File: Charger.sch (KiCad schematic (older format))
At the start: 84 parts, among them Q1 VBA2625, Q10 AON7400A, Q11 AON7400A, Q14 2n7002K, Q15 VBA2625, Q8 AON7400A, Q9 AON7400A, U1 BQ25703ARSNR

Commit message: Much layout. Wow
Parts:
- removed Q10, Q11, Q9: AON7400A, lc_lib:QFN-8_3X3X065P, symbol SmartBattery:AO4468
- added Q10, Q11, Q9: AON7400A, lc_lib:SON-8_3.3X3.3MM, symbol SmartBattery:AON7400A
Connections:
- net VSYS: now also Q11.5 (D), Q11.6 (D), Q11.7 (D), Q11.8 (D)
- net at C15.2, C17.2, C37.1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: now also Q9.5 (D), Q9.6 (D), Q9.7 (D), Q9.8 (D)
- net at C46.1, L1.1, U1.23 (SW2): now also Q10.5 (D), Q10.6 (D), Q10.7 (D), Q10.8 (D), Q11.1 (S), Q11.2 (S), Q11.3 (S)
- net at C43.1, L1.2, Q8.0 (D)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: now also Q9.1 (S), Q9.2 (S), Q9.3 (S)
- net at R38.1: now also Q9.4 (G)
- net at R54.2: now also Q11.4 (G)
- new net: Q10.1 (S), Q10.2 (S), Q10.3 (S)
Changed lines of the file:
@@
-$EndComp
-$Comp
-L SmartBattery:AO4468 Q9
-U 1 1 60390F2A
-P 4050 1950
-F 0 "Q9" V 4393 1950 50  0000 C CNN
-F 1 "AON7400A " V 4302 1950 50  0000 C CNN
-F 2 "lc_lib:QFN-8_3X3X065P" H 4250 2050 50  0001 C CNN
-F 3 "~" H 4050 1950 50  0001 C CNN
-F 4 " C85734" V 4050 1950 50  0001 C CNN "LCSC"
-	1    4050 1950
-	0    -1   -1   0
-$EndComp
-$Comp
-L SmartBattery:AO4468 Q11
-U 1 1 603A292B
-P 6400 2450
-F 0 "Q11" H 6606 2496 50  0000 L CNN
-F 1 "AON7400A " H 6606 2405 50  0000 L CNN
-F 2 "lc_lib:QFN-8_3X3X065P" H 6600 2550 50  0001 C CNN
-F 3 "~" H 6400 2450 50  0001 C CNN
-F 4 "C85734" H 6400 2450 50  0001 C CNN "LCSC"
-	1    6400 2450
-	1    0    0    1
 $EndComp
 $Comp
@@
 	5200 2650 5200 2900
 $Comp
-L SmartBattery:AO4468 Q10
-U 1 1 603A12F1
-P 5600 2050
-F 0 "Q10" H 5806 2096 50  0000 L CNN
-F 1 "AON7400A " H 5806 2005 50  0000 L CNN
-F 2 "lc_lib:QFN-8_3X3X065P" H 5800 2150 50  0001 C CNN
-F 3 "~" H 5600 2050 50  0001 C CNN
-F 4 "C85734" H 5600 2050 50  0001 C CNN "LCSC"
-	1    5600 2050
-	1    0    0    -1
-$EndComp
-$Comp
 L Device:C_Small C51
 U 1 1 6081E24F
@@
 	0    1    1    0
 $EndComp
-Wire Wire Line
-	5200 1850 5700 1850
-Connection ~ 5700 1850
 $Comp
 L power:GND #PWR0128
@@
 Wire Wire Line
 	5750 2250 5700 2250
-Connection ~ 5700 2250
 Wire Wire Line
 	5500 2250 5450 2250
@@
 Wire Wire Line
 	6500 1850 6500 2250
-Wire Wire Line
-	5700 1850 6500 1850
 Wire Wire Line
 	5450 3200 5950 3200
@@
 Wire Wire Line
 	7300 3400 7250 3400
+$Comp
+L SmartBattery:AON7400A Q?
+U 1 1 60093DF8
+P 4050 1950
+AR Path="/5FD15753/60093DF8" Ref="Q?"  Part="1"
+AR Path="/5FD99B08/60093DF8" Ref="Q9"  Part="1"
+F 0 "Q9" V 4400 2100 50  0000 L CNN
+F 1 "AON7400A" V 4300 1900 50  0000 L CNN
+F 2 "lc_lib:SON-8_3.3X3.3MM" H 4700 2400 50  0001 C CNN
+F 3 "~" H 4050 1950 50  0001 C CNN
+F 4 "AON7400A" H 4256 1905 50  0001 L CNN "SKU"
+F 5 "C85734" H 4256 1814 50  0001 L CNN "LCSC"
+	1    4050 1950
+	0    -1   -1   0
+$EndComp
+$Comp
+L SmartBattery:AON7400A Q?
+U 1 1 600966B5
+P 5550 2050
+AR Path="/5FD15753/600966B5" Ref="Q?"  Part="1"
+AR Path="/5FD99B08/600966B5" Ref="Q10"  Part="1"
+F 0 "Q10" V 5900 2200 50  0000 L CNN
+F 1 "AON7400A" V 5800 2000 50  0000 L CNN
+F 2 "lc_lib:SON-8_3.3X3.3MM" H 6200 2500 50  0001 C CNN
+F 3 "~" H 5550 2050 50  0001 C CNN
+F 4 "AON7400A" H 5756 2005 50  0001 L CNN "SKU"
+F 5 "C85734" H 5756 1914 50  0001 L CNN "LCSC"
+	1    5550 2050
+	1    0    0    -1
+$EndComp
+$Comp
+L SmartBattery:AON7400A Q?
+U 1 1 600C3E3E
+P 6400 2450
+AR Path="/5FD15753/600C3E3E" Ref="Q?"  Part="1"
+AR Path="/5FD99B08/600C3E3E" Ref="Q11"  Part="1"
+F 0 "Q11" V 6750 2600 50  0000 L CNN
+F 1 "AON7400A" V 6650 2400 50  0000 L CNN
+F 2 "lc_lib:SON-8_3.3X3.3MM" H 7050 2900 50  0001 C CNN
+F 3 "~" H 6400 2450 50  0001 C CNN
+F 4 "AON7400A" H 6606 2405 50  0001 L CNN "SKU"
+F 5 "C85734" H 6606 2314 50  0001 L CNN "LCSC"
+	1    6400 2450
+	1    0    0    1
+$EndComp
+Wire Wire Line
+	5200 1850 5650 1850
+Connection ~ 5650 1850
+Wire Wire Line
+	5650 1850 6500 1850
 $EndSCHEMATC

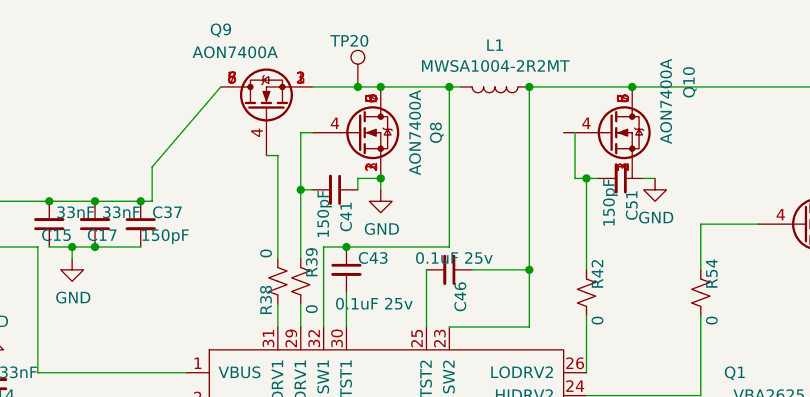
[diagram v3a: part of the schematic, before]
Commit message: Layout placed type-c + barrel jack
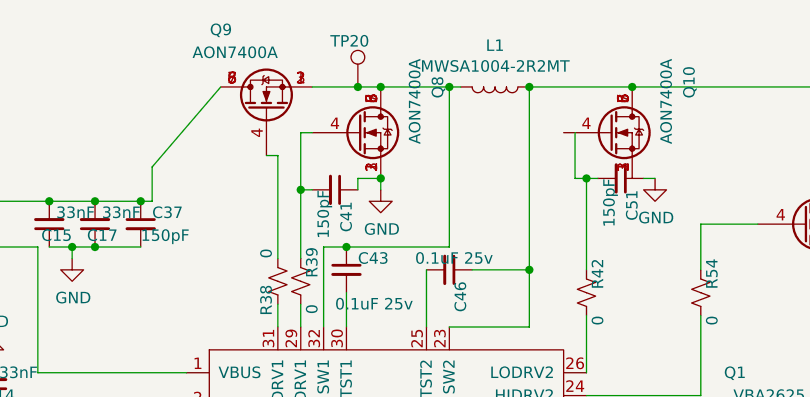
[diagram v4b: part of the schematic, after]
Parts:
- removed Q8: AON7400A, lc_lib:QFN-8_3X3X065P, symbol SmartBattery:AO4468
- added Q8: AON7400A, lc_lib:SON-8_3.3X3.3MM, symbol SmartBattery:AON7400A
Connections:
- net GND: now also Q8.1 (S), Q8.2 (S), Q8.3 (S)
- net at C43.1, L1.2, Q9.1 (S)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: now also Q8.5 (D), Q8.6 (D), Q8.7 (D), Q8.8 (D)
- net at C41.2, R39.2: now also Q8.4 (G)
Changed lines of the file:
@@
 	3500 2550 3300 2550
 Connection ~ 3300 2550
-$Comp
-L SmartBattery:AO4468 Q8
-U 1 1 6038DB58
-P 4450 2050
-F 0 "Q8" V 4793 2050 50  0000 C CNN
-F 1 "AON7400A " V 4702 2050 50  0000 C CNN
-F 2 "lc_lib:QFN-8_3X3X065P" H 4650 2150 50  0001 C CNN
-F 3 "~" H 4450 2050 50  0001 C CNN
-F 4 "C85734" V 4450 2050 50  0001 C CNN "LCSC"
-	1    4450 2050
-	1    0    0    -1
-$EndComp
 Wire Wire Line
 	3550 2350 3550 2200
@@
 Wire Wire Line
 	4450 2250 4450 2300
-Connection ~ 4550 2250
 Wire Wire Line
 	4250 2300 4200 2300
@@
 $EndComp
 Connection ~ 4450 1850
-Wire Wire Line
-	4450 1850 4550 1850
-Wire Wire Line
-	4550 1850 4850 1850
-Connection ~ 4550 1850
 Wire Wire Line
 	4300 2900 4300 2550
@@
 Wire Wire Line
 	5650 1850 6500 1850
+$Comp
+L SmartBattery:AON7400A Q?
+U 1 1 600EE040
+P 4450 2050
+AR Path="/5FD15753/600EE040" Ref="Q?"  Part="1"
+AR Path="/5FD99B08/600EE040" Ref="Q8"  Part="1"
+F 0 "Q8" V 4800 2200 50  0000 L CNN
+F 1 "AON7400A" V 4700 2000 50  0000 L CNN
+F 2 "lc_lib:SON-8_3.3X3.3MM" H 5100 2500 50  0001 C CNN
+F 3 "~" H 4450 2050 50  0001 C CNN
+F 4 "AON7400A" H 4656 2005 50  0001 L CNN "SKU"
+F 5 "C85734" H 4656 1914 50  0001 L CNN "LCSC"
+	1    4450 2050
+	1    0    0    -1
+$EndComp
+Wire Wire Line
+	4450 1850 4550 1850
+Connection ~ 4550 2250
+Connection ~ 4550 1850
+Wire Wire Line
+	4550 1850 4850 1850
 $EndSCHEMATC

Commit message: Much layout wow.
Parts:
- removed C16, C89: 220u, Capacitor_SMD:C_Elec_8x10.2, symbol Device:C_Small
- added C147, C16, C89: 220u, Capacitor_SMD:C_Elec_8x10.2, symbol Device:CP_Small
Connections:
- net ADAPTER_IN: now also C147.1
- net GND: now also Q10.1 (S), Q10.2 (S), Q10.3 (S), C147.2, C16.2, C89.2
- net VSYS: now also C16.1, C89.1
- net at Q10.4 (G): now also C51.2, R42.2
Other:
- moved on the sheet: C51
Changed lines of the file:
@@
 	0    -1   -1   0
-$EndComp
-$Comp
-L Device:C_Small C16
-U 1 1 5FDC314F
-P 7950 2800
-F 0 "C16" H 8042 2846 50  0000 L CNN
-F 1 "220u" H 8042 2755 50  0000 L CNN
-F 2 "Capacitor_SMD:C_Elec_8x10.2" H 7950 2800 50  0001 C CNN
-F 3 "~" H 7950 2800 50  0001 C CNN
-F 4 "C311611" H 7950 2800 50  0001 C CNN "LCSC"
-	1    7950 2800
-	1    0    0    -1
 $EndComp
 Text HLabel 8400 2500 2    50   BiDi ~ 0
@@
 L Device:C_Small C51
 U 1 1 6081E24F
-P 5600 2250
-F 0 "C51" H 5650 2300 50  0000 L CNN
-F 1 "150pF" H 5600 2200 50  0000 L CNN
-F 2 "lc_lib:0402_C" H 5600 2250 50  0001 C CNN
-F 3 "~" H 5600 2250 50  0001 C CNN
-F 4 "C1527" H 5600 2250 50  0001 C CNN "lcsc"
-	1    5600 2250
+P 5550 2350
+F 0 "C51" H 5600 2400 50  0000 L CNN
+F 1 "150pF" H 5550 2300 50  0000 L CNN
+F 2 "lc_lib:0402_C" H 5550 2350 50  0001 C CNN
+F 3 "~" H 5550 2350 50  0001 C CNN
+F 4 "C1527" H 5550 2350 50  0001 C CNN "lcsc"
+	1    5550 2350
 	0    1    1    0
 $EndComp
@@
 $EndComp
 Wire Wire Line
-	5750 2250 5700 2250
-Wire Wire Line
-	5500 2250 5450 2250
-Wire Wire Line
 	5400 2250 5400 2050
 Wire Wire Line
 	5450 3100 5450 2850
-Connection ~ 5450 2250
 Wire Wire Line
 	5450 2250 5400 2250
@@
 $EndComp
 Wire Wire Line
-	5450 2650 5450 2250
+	5450 2650 5450 2350
 $Comp
 L Device:R_Small_US R54
@@
 	1    0    0    -1
 $EndComp
-$Comp
-L Device:C_Small C89
-U 1 1 60904FCD
-P 8300 2800
-F 0 "C89" H 8392 2846 50  0000 L CNN
-F 1 "220u" H 8392 2755 50  0000 L CNN
-F 2 "Capacitor_SMD:C_Elec_8x10.2" H 8300 2800 50  0001 C CNN
-F 3 "~" H 8300 2800 50  0001 C CNN
-F 4 "C311611" H 8300 2800 50  0001 C CNN "LCSC"
-	1    8300 2800
-	1    0    0    -1
-$EndComp
 Wire Wire Line
 	6800 2900 6950 2900
@@
 Wire Wire Line
 	7700 2900 7800 2900
-Connection ~ 7950 2900
-Wire Wire Line
-	7950 2900 8300 2900
 Wire Wire Line
 	7250 2700 7400 2700
@@
 	7400 2700 7500 2700
 Connection ~ 7700 2700
-Wire Wire Line
-	7700 2700 7950 2700
-Connection ~ 7950 2700
-Wire Wire Line
-	7950 2700 8300 2700
 $Comp
 L power:GND #PWR0129
@@
 $EndComp
 Connection ~ 7800 2900
-Wire Wire Line
-	7800 2900 7950 2900
 Connection ~ 7500 2700
 Wire Wire Line
@@
 Wire Wire Line
 	8300 2500 8400 2500
-Connection ~ 8300 2700
 Wire Wire Line
 	6800 3400 6550 3400
@@
 Wire Wire Line
 	4550 1850 4850 1850
+Wire Wire Line
+	2400 3550 2600 3550
+Connection ~ 2400 3550
+Wire Wire Line
+	2600 3750 2400 3750
+Connection ~ 2400 3750
+$Comp
+L Device:CP_Small C?
+U 1 1 600ECC91
+P 2600 3650
+AR Path="/60413DD6/600ECC91" Ref="C?"  Part="1"
+AR Path="/5FD99B08/600ECC91" Ref="C147"  Part="1"
+F 0 "C147" H 2500 3700 50  0000 R CNN
+F 1 "220u" H 2450 3600 50  0000 R CNN
+F 2 "Capacitor_SMD:C_Elec_8x10.2" H 2600 3650 50  0001 C CNN
+F 3 "~" H 2600 3650 50  0001 C CNN
+F 4 "C311611" H 2600 3650 50  0001 C CNN "LCSC"
+	1    2600 3650
+	-1   0    0    -1
+$EndComp
+$Comp
+L Device:CP_Small C?
+U 1 1 600F8E33
+P 8000 2800
+AR Path="/60413DD6/600F8E33" Ref="C?"  Part="1"
+AR Path="/5FD99B08/600F8E33" Ref="C16"  Part="1"
+F 0 "C16" H 7900 2850 50  0000 R CNN
+F 1 "220u" H 7900 2750 50  0000 R CNN
+F 2 "Capacitor_SMD:C_Elec_8x10.2" H 8000 2800 50  0001 C CNN
+F 3 "~" H 8000 2800 50  0001 C CNN
+F 4 "C311611" H 8000 2800 50  0001 C CNN "LCSC"
+	1    8000 2800
+	-1   0    0    -1
+$EndComp
+$Comp
+L Device:CP_Small C?
+U 1 1 600FA944
+P 8300 2800
+AR Path="/60413DD6/600FA944" Ref="C?"  Part="1"
+AR Path="/5FD99B08/600FA944" Ref="C89"  Part="1"
+F 0 "C89" H 8200 2850 50  0000 R CNN
+F 1 "220u" H 8150 2750 50  0000 R CNN
+F 2 "Capacitor_SMD:C_Elec_8x10.2" H 8300 2800 50  0001 C CNN
+F 3 "~" H 8300 2800 50  0001 C CNN
+F 4 "C311611" H 8300 2800 50  0001 C CNN "LCSC"
+	1    8300 2800
+	-1   0    0    -1
+$EndComp
+Wire Wire Line
+	7700 2700 8000 2700
+Wire Wire Line
+	7800 2900 8000 2900
+Connection ~ 8000 2700
+Wire Wire Line
+	8000 2700 8300 2700
+Connection ~ 8000 2900
+Wire Wire Line
+	8000 2900 8300 2900
+Connection ~ 8300 2700
+Wire Wire Line
+	5400 2050 5350 2050
+Connection ~ 5450 2350
+Wire Wire Line
+	5450 2350 5450 2250
+Wire Wire Line
+	5650 2250 5750 2250
+Connection ~ 5650 2250
+Wire Wire Line
+	5650 2250 5650 2350
 $EndSCHEMATC

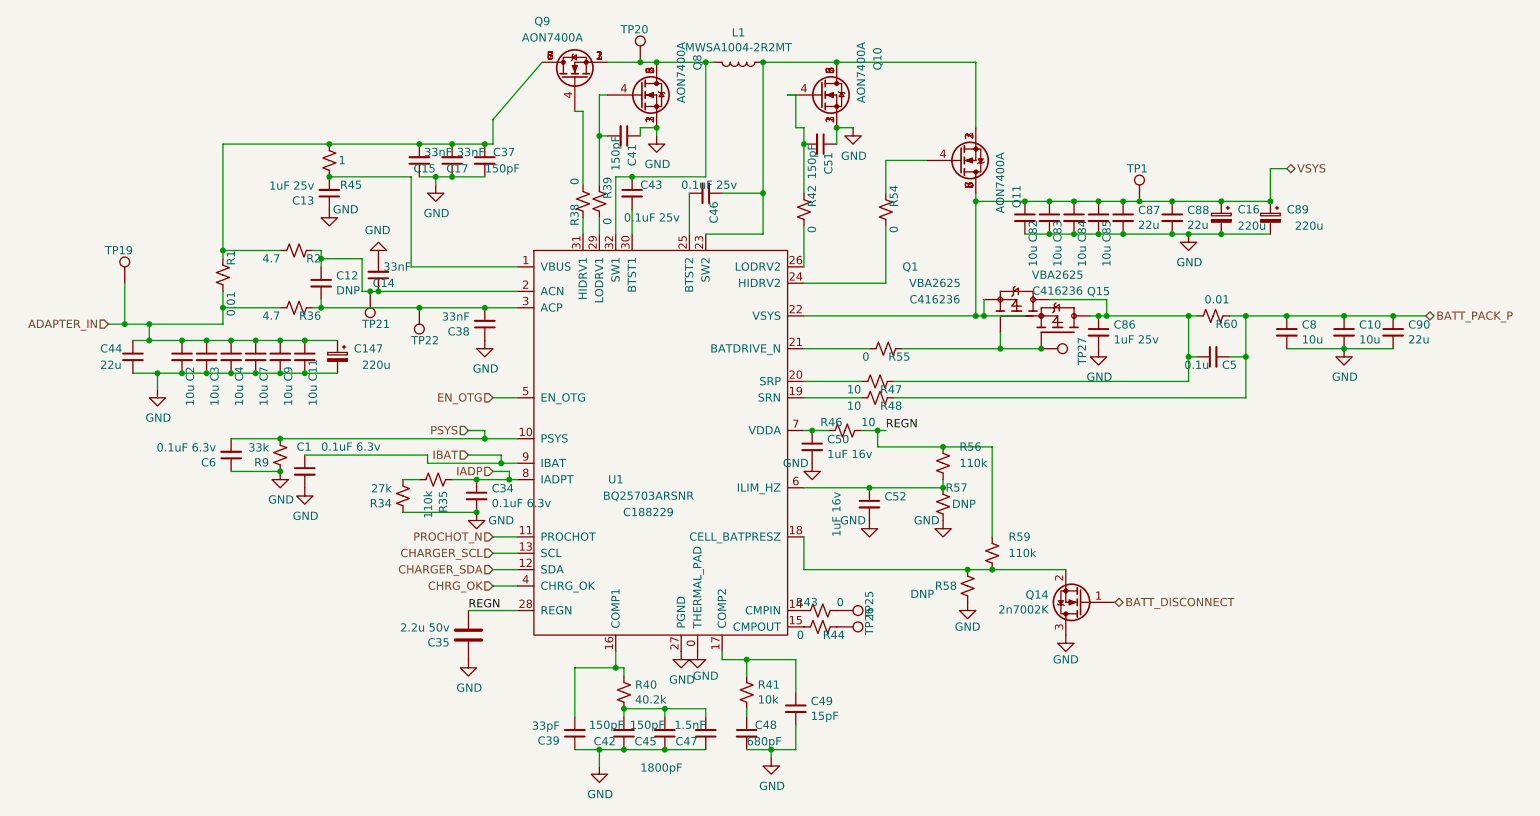
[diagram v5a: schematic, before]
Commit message: Almost connected MCU + ESP32 added leds addedd uart usb cleaned up type-c I/O -- STILL NEED TO level shift I2C
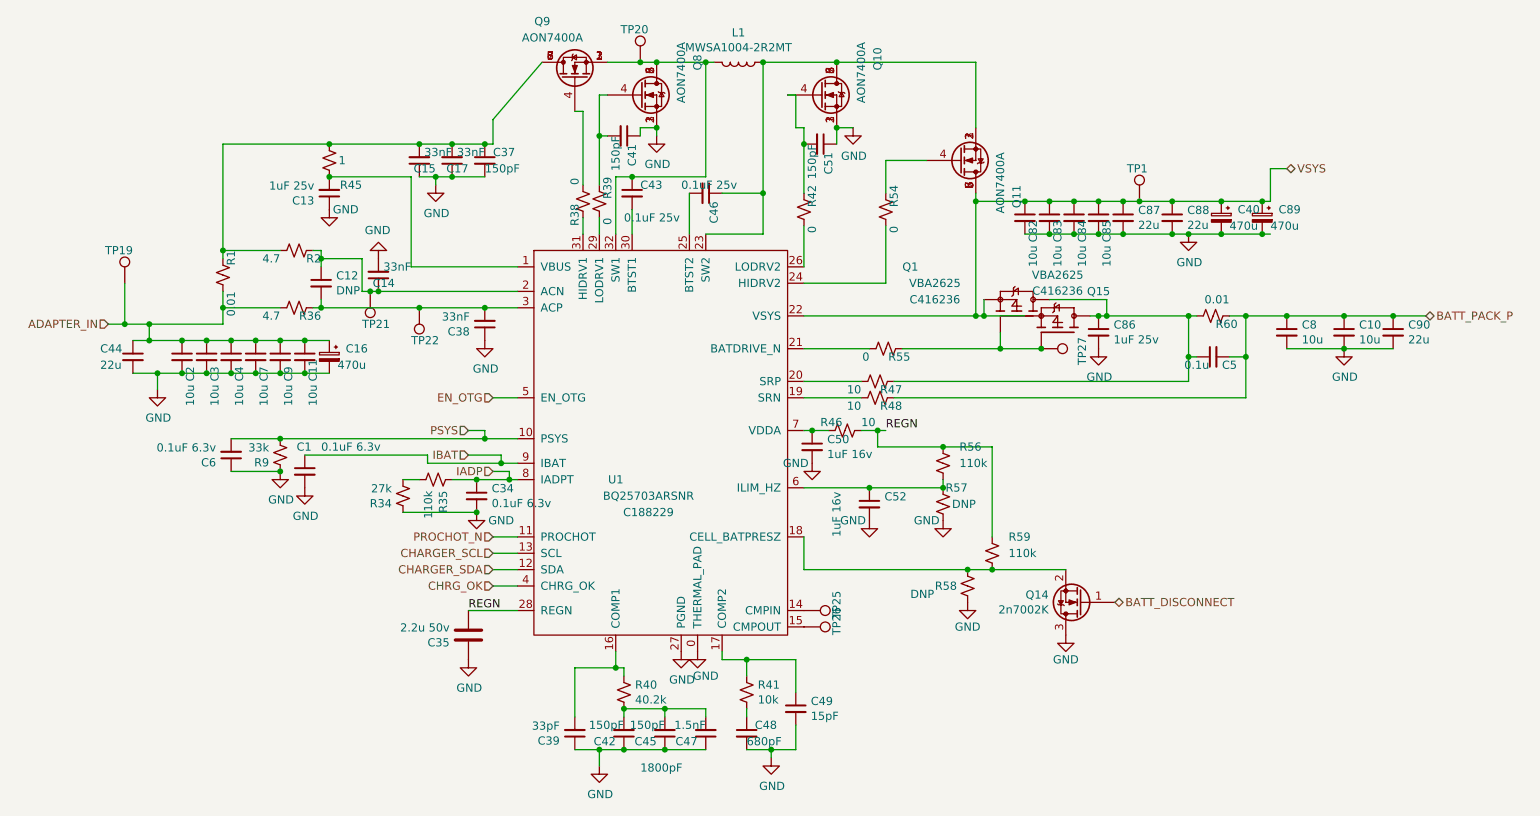
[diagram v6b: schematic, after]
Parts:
- removed C147: 220u, Capacitor_SMD:C_Elec_8x10.2, symbol Device:CP_Small
- removed R43, R44: 0, lc_lib:0402_R, symbol Device:R_Small_US
- added C40: 470u, Capacitor_SMD:C_Elec_10x10.2, symbol Device:CP_Small
- C16, C89: value 220u -> 470u; footprint Capacitor_SMD:C_Elec_8x10.2 -> Capacitor_SMD:C_Elec_10x10.2; LCSC C311611 -> C72519; pn (none) -> RVT1V471M1010
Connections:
- net ADAPTER_IN: now also C16.1
- net GND: now also C40.2
- net VSYS: now also C40.1; no longer C16.1
- net at U1.14 (CMPIN): now also TP25.1
- net at U1.15 (CMPOUT): now also TP26.1
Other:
- moved on the sheet: TP25, TP26
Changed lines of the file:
@@
-$EndComp
-$Comp
-L Device:R_Small_US R44
-U 1 1 60AFFAA9
-P 5550 5300
-AR Path="/5FD99B08/60AFFAA9" Ref="R44"  Part="1"
-AR Path="/5FF1D194/60AFFAA9" Ref="R?"  Part="1"
-F 0 "R44" V 5500 5150 50  0000 L CNN
-F 1 "0" V 5500 5400 50  0000 L CNN
-F 2 "lc_lib:0402_R" H 5550 5300 50  0001 C CNN
-F 3 "~" H 5550 5300 50  0001 C CNN
-	1    5550 5300
-	0    -1   -1   0
-$EndComp
-$Comp
-L Device:R_Small_US R43
-U 1 1 60B01311
-P 5550 5200
-AR Path="/5FD99B08/60B01311" Ref="R43"  Part="1"
-AR Path="/5FF1D194/60B01311" Ref="R?"  Part="1"
-F 0 "R43" V 5500 5050 50  0000 L CNN
-F 1 "0" V 5500 5300 50  0000 L CNN
-F 2 "lc_lib:0402_R" H 5550 5200 50  0001 C CNN
-F 3 "~" H 5550 5200 50  0001 C CNN
-	1    5550 5200
-	0    1    1    0
 $EndComp
 $Comp
 L Connector:TestPoint TP?
 U 1 1 60B017C9
-P 5650 5200
+P 5450 5200
 AR Path="/5FD15753/60B017C9" Ref="TP?"  Part="1"
 AR Path="/5FD99B08/60B017C9" Ref="TP25"  Part="1"
-F 0 "TP25" H 5700 5400 50  0000 R CNN
-F 1 "TestPoint" H 5100 5250 50  0001 R CNN
-F 2 "TestPoint:TestPoint_Pad_D2.0mm" H 5850 5200 50  0001 C CNN
-F 3 "~" H 5850 5200 50  0001 C CNN
-	1    5650 5200
+F 0 "TP25" H 5500 5400 50  0000 R CNN
+F 1 "TestPoint" H 4900 5250 50  0001 R CNN
+F 2 "TestPoint:TestPoint_Pad_D2.0mm" H 5650 5200 50  0001 C CNN
+F 3 "~" H 5650 5200 50  0001 C CNN
+	1    5450 5200
 	0    1    1    0
 $EndComp
@@
 L Connector:TestPoint TP?
 U 1 1 60B02C85
-P 5650 5300
+P 5450 5300
 AR Path="/5FD15753/60B02C85" Ref="TP?"  Part="1"
 AR Path="/5FD99B08/60B02C85" Ref="TP26"  Part="1"
-F 0 "TP26" H 5700 5500 50  0000 R CNN
-F 1 "TestPoint" H 5100 5350 50  0001 R CNN
-F 2 "TestPoint:TestPoint_Pad_D2.0mm" H 5850 5300 50  0001 C CNN
-F 3 "~" H 5850 5300 50  0001 C CNN
-	1    5650 5300
+F 0 "TP26" H 5500 5500 50  0000 R CNN
+F 1 "TestPoint" H 4900 5350 50  0001 R CNN
+F 2 "TestPoint:TestPoint_Pad_D2.0mm" H 5650 5300 50  0001 C CNN
+F 3 "~" H 5650 5300 50  0001 C CNN
+	1    5450 5300
 	0    1    1    0
 $EndComp
@@
 	4550 1850 4850 1850
 Wire Wire Line
-	2400 3550 2600 3550
+	2400 3550 2550 3550
 Connection ~ 2400 3550
-Wire Wire Line
-	2600 3750 2400 3750
 Connection ~ 2400 3750
+Wire Wire Line
+	5400 2050 5350 2050
+Connection ~ 5450 2350
+Wire Wire Line
+	5450 2350 5450 2250
+Wire Wire Line
+	5650 2250 5750 2250
+Connection ~ 5650 2250
+Wire Wire Line
+	5650 2250 5650 2350
 $Comp
 L Device:CP_Small C?
-U 1 1 600ECC91
-P 2600 3650
-AR Path="/60413DD6/600ECC91" Ref="C?"  Part="1"
-AR Path="/5FD99B08/600ECC91" Ref="C147"  Part="1"
-F 0 "C147" H 2500 3700 50  0000 R CNN
-F 1 "220u" H 2450 3600 50  0000 R CNN
-F 2 "Capacitor_SMD:C_Elec_8x10.2" H 2600 3650 50  0001 C CNN
-F 3 "~" H 2600 3650 50  0001 C CNN
-F 4 "C311611" H 2600 3650 50  0001 C CNN "LCSC"
-	1    2600 3650
-	-1   0    0    -1
-$EndComp
-$Comp
-L Device:CP_Small C?
-U 1 1 600F8E33
+U 1 1 60282998
 P 8000 2800
-AR Path="/60413DD6/600F8E33" Ref="C?"  Part="1"
-AR Path="/5FD99B08/600F8E33" Ref="C16"  Part="1"
-F 0 "C16" H 7900 2850 50  0000 R CNN
-F 1 "220u" H 7900 2750 50  0000 R CNN
-F 2 "Capacitor_SMD:C_Elec_8x10.2" H 8000 2800 50  0001 C CNN
+AR Path="/60413DD6/60282998" Ref="C?"  Part="1"
+AR Path="/5FD99B08/60282998" Ref="C40"  Part="1"
+F 0 "C40" H 7900 2850 50  0000 R CNN
+F 1 "470u" H 7950 2750 50  0000 R CNN
+F 2 "Capacitor_SMD:C_Elec_10x10.2" H 8000 2800 50  0001 C CNN
 F 3 "~" H 8000 2800 50  0001 C CNN
-F 4 "C311611" H 8000 2800 50  0001 C CNN "LCSC"
+F 4 "C72519" H 8000 2800 50  0001 C CNN "LCSC"
+F 5 "RVT1V471M1010" H 8000 2800 50  0001 C CNN "pn"
 	1    8000 2800
 	-1   0    0    -1
 $EndComp
-$Comp
-L Device:CP_Small C?
-U 1 1 600FA944
-P 8300 2800
-AR Path="/60413DD6/600FA944" Ref="C?"  Part="1"
-AR Path="/5FD99B08/600FA944" Ref="C89"  Part="1"
-F 0 "C89" H 8200 2850 50  0000 R CNN
-F 1 "220u" H 8150 2750 50  0000 R CNN
-F 2 "Capacitor_SMD:C_Elec_8x10.2" H 8300 2800 50  0001 C CNN
-F 3 "~" H 8300 2800 50  0001 C CNN
-F 4 "C311611" H 8300 2800 50  0001 C CNN "LCSC"
-	1    8300 2800
-	-1   0    0    -1
-$EndComp
 Wire Wire Line
 	7700 2700 8000 2700
@@
 Connection ~ 8000 2700
 Wire Wire Line
-	8000 2700 8300 2700
+	8000 2700 8250 2700
 Connection ~ 8000 2900
 Wire Wire Line
-	8000 2900 8300 2900
-Connection ~ 8300 2700
-Wire Wire Line
-	5400 2050 5350 2050
-Connection ~ 5450 2350
-Wire Wire Line
-	5450 2350 5450 2250
-Wire Wire Line
-	5650 2250 5750 2250
-Connection ~ 5650 2250
-Wire Wire Line
-	5650 2250 5650 2350
+	8000 2900 8250 2900
+$Comp
+L Device:CP_Small C?
+U 1 1 60283D8F
+P 8250 2800
+AR Path="/60413DD6/60283D8F" Ref="C?"  Part="1"
+AR Path="/5FD99B08/60283D8F" Ref="C89"  Part="1"
+F 0 "C89" H 8150 2850 50  0000 R CNN
+F 1 "470u" H 8200 2750 50  0000 R CNN
+F 2 "Capacitor_SMD:C_Elec_10x10.2" H 8250 2800 50  0001 C CNN
+F 3 "~" H 8250 2800 50  0001 C CNN
+F 4 "C72519" H 8250 2800 50  0001 C CNN "LCSC"
+F 5 "RVT1V471M1010" H 8250 2800 50  0001 C CNN "pn"
+	1    8250 2800
+	-1   0    0    -1
+$EndComp
+Connection ~ 8250 2700
+Wire Wire Line
+	8250 2700 8300 2700
+Connection ~ 8250 2900
+Wire Wire Line
+	8250 2900 8300 2900
+$Comp
+L Device:CP_Small C?
+U 1 1 6028423D
+P 2550 3650
+AR Path="/60413DD6/6028423D" Ref="C?"  Part="1"
+AR Path="/5FD99B08/6028423D" Ref="C16"  Part="1"
+F 0 "C16" H 2450 3700 50  0000 R CNN
+F 1 "470u" H 2500 3600 50  0000 R CNN
+F 2 "Capacitor_SMD:C_Elec_10x10.2" H 2550 3650 50  0001 C CNN
+F 3 "~" H 2550 3650 50  0001 C CNN
+F 4 "C72519" H 2550 3650 50  0001 C CNN "LCSC"
+F 5 "RVT1V471M1010" H 2550 3650 50  0001 C CNN "pn"
+	1    2550 3650
+	-1   0    0    -1
+$EndComp
+Wire Wire Line
+	2550 3750 2400 3750
 $EndSCHEMATC
